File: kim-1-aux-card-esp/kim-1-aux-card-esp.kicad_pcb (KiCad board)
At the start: 2 copper layers, 64.3 x 110.7 mm, 33 parts, among them J1 Motherboard, J10 PRG_HDR, J2 SD_Shield, J3 DIN-6, J4 Reset, J5 GND, J6 +5V, J8 RUN_FLASH, J9 RUN_FLASH, Q1 PN2222A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

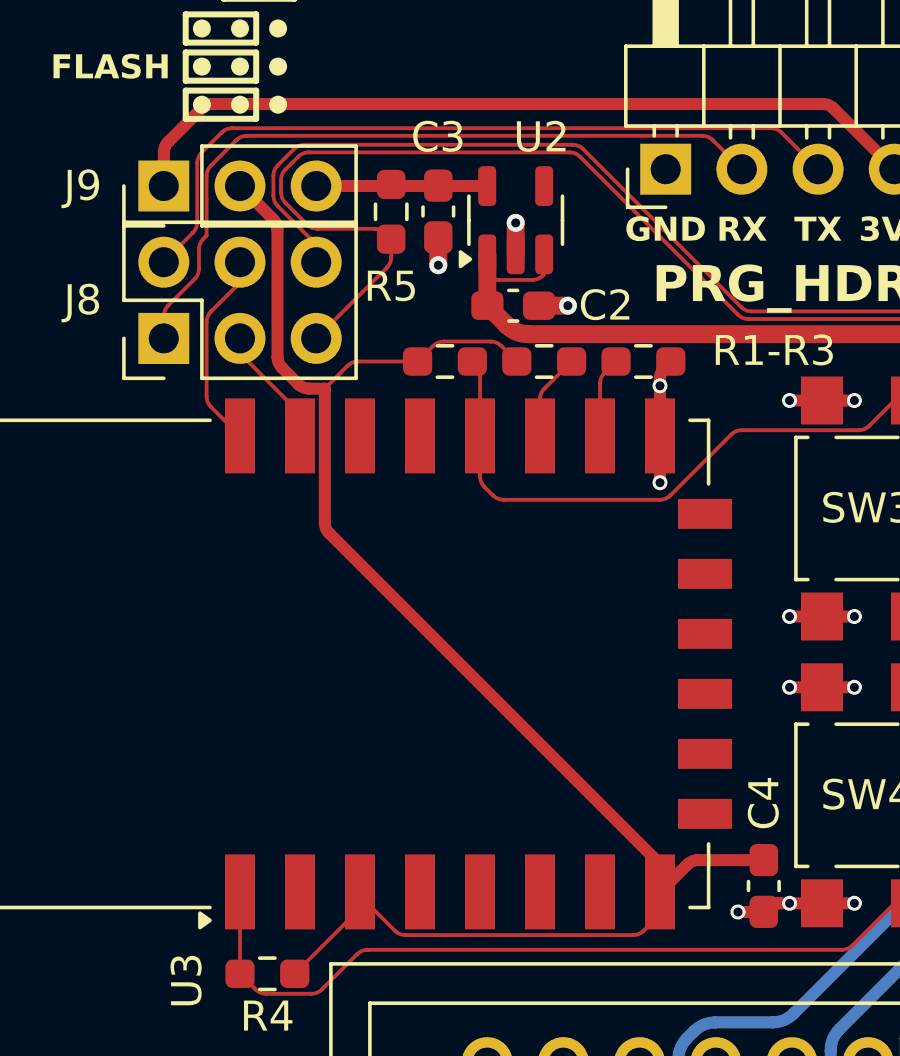
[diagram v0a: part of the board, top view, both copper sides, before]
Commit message: Minor trace optimizations
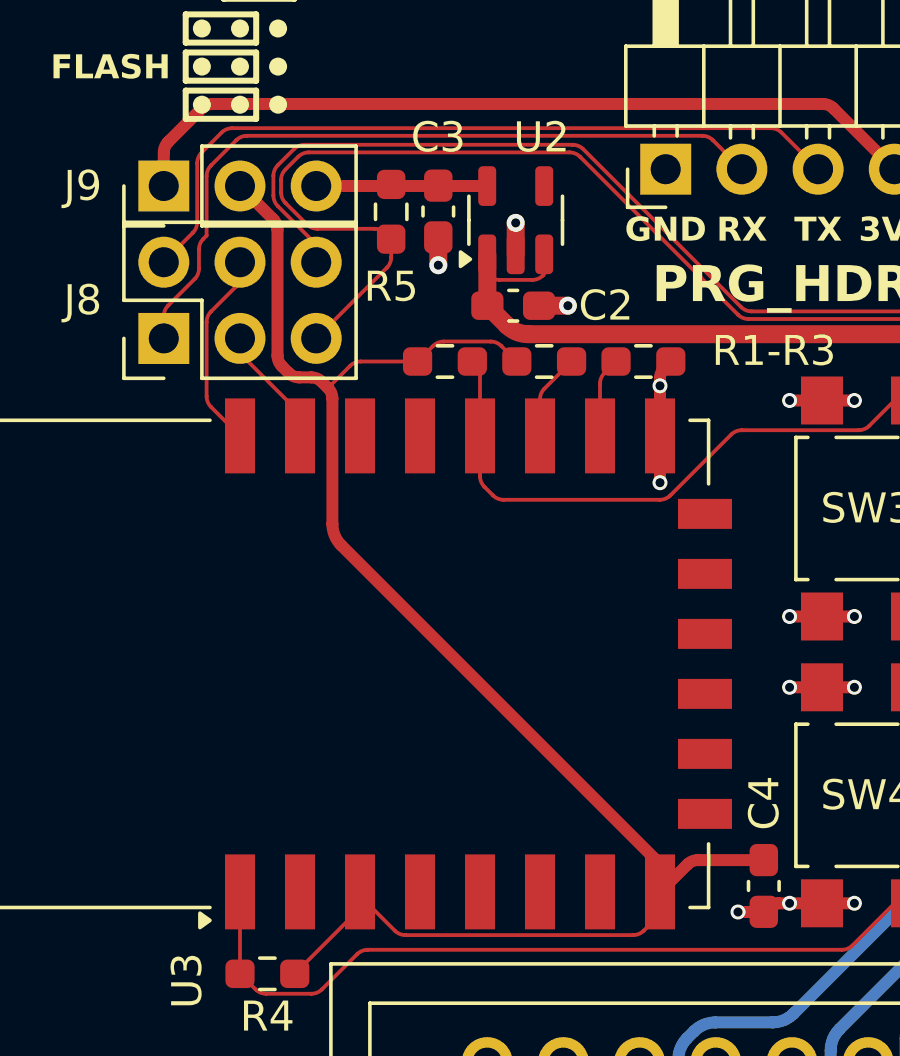
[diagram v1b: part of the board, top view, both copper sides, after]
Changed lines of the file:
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@@
   (segment (start 123.986607 76.1305) (end 131.572393 76.1305) (width 0.127) (layer "F.Cu") (net 3))
   (segment (start 124.39 57.01) (end 124.909054 56.490946) (width 0.127) (layer "F.Cu") (net 3))
-  (segment (start 120.770107 57.913) (end 121.297 57.913) (width 0.4) (layer "F.Cu") (net 3))
-  (segment (start 121.297 57.913) (end 121.297 62.379893) (width 0.4) (layer "F.Cu") (net 3))
+  (segment (start 124.39 57.01) (end 122.494213 57.01) (width 0.127) (layer "F.Cu") (net 3))
   (segment (start 122.47 74.69) (end 122.47 74.559) (width 0.127) (layer "F.Cu") (net 3))
   (segment (start 135.93 73.63) (end 133.737107 73.63) (width 0.4) (layer "F.Cu") (net 3))
-  (segment (start 124.39 57.01) (end 122.407107 57.01) (width 0.127) (layer "F.Cu") (net 3))
+  (segment (start 120.093553 57.393553) (end 119.866446 57.166446) (width 0.4) (layer "F.Cu") (net 3))
   (segment (start 122.47 75.037893) (end 122.47 74.69) (width 0.127) (layer "F.Cu") (net 3))
-  (segment (start 119.72 52.617107) (end 119.72 56.862893) (width 0.4) (layer "F.Cu") (net 3))
   (segment (start 125.262607 56.3445) (end 126.824893 56.3445) (width 0.127) (layer "F.Cu") (net 3))
   (segment (start 122.47 74.821) (end 123.633054 75.984054) (width 0.127) (layer "F.Cu") (net 3))
+  (segment (start 119.72 56.812893) (end 119.72 52.617107) (width 0.4) (layer "F.Cu") (net 3))
   (segment (start 133.383553 73.776447) (end 132.47 74.69) (width 0.4) (layer "F.Cu") (net 3))
   (segment (start 127.178447 56.490947) (end 127.6975 57.01) (width 0.127) (layer "F.Cu") (net 3))
-  (segment (start 119.866447 57.216447) (end 120.416554 57.766554) (width 0.4) (layer "F.Cu") (net 3))
+  (segment (start 122.140659 57.156447) (end 121.403553 57.893553) (width 0.127) (layer "F.Cu") (net 3))
   (segment (start 132.47 73.967107) (end 132.47 74.69) (width 0.4) (layer "F.Cu") (net 3))
-  (segment (start 118.47 51.16) (end 119.573554 52.263554) (width 0.4) (layer "F.Cu") (net 3))
+  (segment (start 119.573554 52.263554) (end 118.47 51.16) (width 0.4) (layer "F.Cu") (net 3))
+  (segment (start 121.842893 63.132893) (end 132.323554 73.613554) (width 0.4) (layer "F.Cu") (net 3))
+  (segment (start 121.403553 57.893553) (end 121.196446 57.686446) (width 0.4) (layer "F.Cu") (net 3))
   (segment (start 127.6975 57.01) (end 127.521471 57.01) (width 0.127) (layer "F.Cu") (net 3))
   (segment (start 132.47 75.232893) (end 132.47 74.69) (width 0.127) (layer "F.Cu") (net 3))
+  (segment (start 121.55 58.247107) (end 121.55 62.425786) (width 0.4) (layer "F.Cu") (net 3))
   (segment (start 131.925947 75.984053) (end 132.323554 75.586446) (width 0.127) (layer "F.Cu") (net 3))
+  (segment (start 120.842893 57.54) (end 120.447107 57.54) (width 0.4) (layer "F.Cu") (net 3))
   (segment (start 122.47 74.69) (end 122.47 74.821) (width 0.127) (layer "F.Cu") (net 3))
-  (segment (start 122.053553 57.156447) (end 121.297 57.913) (width 0.127) (layer "F.Cu") (net 3))
-  (segment (start 121.443447 62.733447) (end 132.323554 73.613554) (width 0.4) (layer "F.Cu") (net 3))
+  (arc (start 122.494213 57.01) (mid 122.302871 57.04806) (end 122.140659 57.156447) (width 0.127) (layer "F.Cu") (net 3))
   (arc (start 122.47 75.037893) (mid 122.43194 75.229234) (end 122.323554 75.391446) (width 0.127) (layer "F.Cu") (net 3))
-  (arc (start 119.72 52.617107) (mid 119.68194 52.425766) (end 119.573554 52.263554) (width 0.4) (layer "F.Cu") (net 3))
-  (arc (start 119.72 56.862893) (mid 119.75806 57.054235) (end 119.866447 57.216447) (width 0.4) (layer "F.Cu") (net 3))
-  (arc (start 132.47 73.967107) (mid 132.43194 73.775766) (end 132.323554 73.613554) (width 0.4) (layer "F.Cu") (net 3))
+  (arc (start 119.72 52.617107) (mid 119.681938 52.425766) (end 119.573554 52.263554) (width 0.4) (layer "F.Cu") (net 3))
+  (arc (start 119.72 56.812893) (mid 119.75806 57.004234) (end 119.866446 57.166446) (width 0.4) (layer "F.Cu") (net 3))
   (arc (start 123.633054 75.984054) (mid 123.795266 76.09244) (end 123.986607 76.1305) (width 0.127) (layer "F.Cu") (net 3))
-  (arc (start 122.053553 57.156447) (mid 122.215765 57.04806) (end 122.407107 57.01) (width 0.127) (layer "F.Cu") (net 3))
   (arc (start 133.383553 73.776447) (mid 133.545765 73.66806) (end 133.737107 73.63) (width 0.4) (layer "F.Cu") (net 3))
-  (arc (start 121.297 62.379893) (mid 121.33506 62.571235) (end 121.443447 62.733447) (width 0.4) (layer "F.Cu") (net 3))
+  (arc (start 120.842893 57.54) (mid 121.034234 57.57806) (end 121.196446 57.686446) (width 0.4) (layer "F.Cu") (net 3))
+  (arc (start 121.55 58.247107) (mid 121.51194 58.055765) (end 121.403553 57.893553) (width 0.4) (layer "F.Cu") (net 3))
   (arc (start 126.824893 56.3445) (mid 127.016235 56.38256) (end 127.178447 56.490947) (width 0.127) (layer "F.Cu") (net 3))
+  (arc (start 120.447107 57.54) (mid 120.255765 57.50194) (end 120.093553 57.393553) (width 0.4) (layer "F.Cu") (net 3))
+  (arc (start 132.323554 73.613554) (mid 132.431942 73.775764) (end 132.47 73.967107) (width 0.4) (layer "F.Cu") (net 3))
+  (arc (start 121.842893 63.132893) (mid 121.62612 62.80847) (end 121.55 62.425786) (width 0.4) (layer "F.Cu") (net 3))
   (arc (start 125.262607 56.3445) (mid 125.071266 56.38256) (end 124.909054 56.490946) (width 0.127) (layer "F.Cu") (net 3))
   (arc (start 131.572393 76.1305) (mid 131.763735 76.09244) (end 131.925947 75.984053) (width 0.127) (layer "F.Cu") (net 3))
-  (arc (start 120.770107 57.913) (mid 120.578766 57.87494) (end 120.416554 57.766554) (width 0.4) (layer "F.Cu") (net 3))
   (arc (start 132.47 75.232893) (mid 132.43194 75.424234) (end 132.323554 75.586446) (width 0.127) (layer "F.Cu") (net 3))
   (segment (start 116.076447 55.144343) (end 116.956054 54.264736) (width 0.127) (layer "F.Cu") (net 4))
